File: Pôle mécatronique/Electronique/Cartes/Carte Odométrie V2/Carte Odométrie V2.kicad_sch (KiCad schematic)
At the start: 10 parts, among them J1 Conn_01x05, J2 Conn_01x08, J3 Conn_01x07, J4 Conn_01x04, J5 Conn_01x07, J6 Conn_01x04, U1 TCAN332

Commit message: MAJ carte actionneur
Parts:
- removed U1: TCAN332, empreinte:SO-8_S, symbol Interface_CAN_LIN:TCAN332
- added C1, C2: C, Capacitor_SMD:C_1206_3216Metric, symbol Device:C
- added R3: R, Resistor_THT:R_Axial_DIN0207_L6.3mm_D2.5mm_P10.16mm_Horizontal, symbol Device:R
- added TP1: TestPoint, TestPoint:TestPoint_Pad_D2.0mm, symbol Connector:TestPoint
- added U1: MCP2551-I-P, Package_DIP:DIP-8_W7.62mm, symbol Interface_CAN_LIN:MCP2551-I-P
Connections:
- net +5V: now also J4.4 (Pin_4), C1.1, C2.1, U1.3 (VDD)
- net CAN_H: now also R3.1, U1.7 (CANH)
- net CAN_L: now also R3.2, U1.6 (CANL)
- net CAN_RX: now also U1.4 (RXD)
- net CAN_TX: now also U1.1 (TXD)
- net GND: now also C1.2, C2.2, TP1.1, U1.2 (VSS), U1.8 (Rs)
- net +BATT: no longer names the net of A1.4.1 (VIN)
- net +BATT: no longer J4.4 (Pin_4)
- no-connect marks 23 -> 25

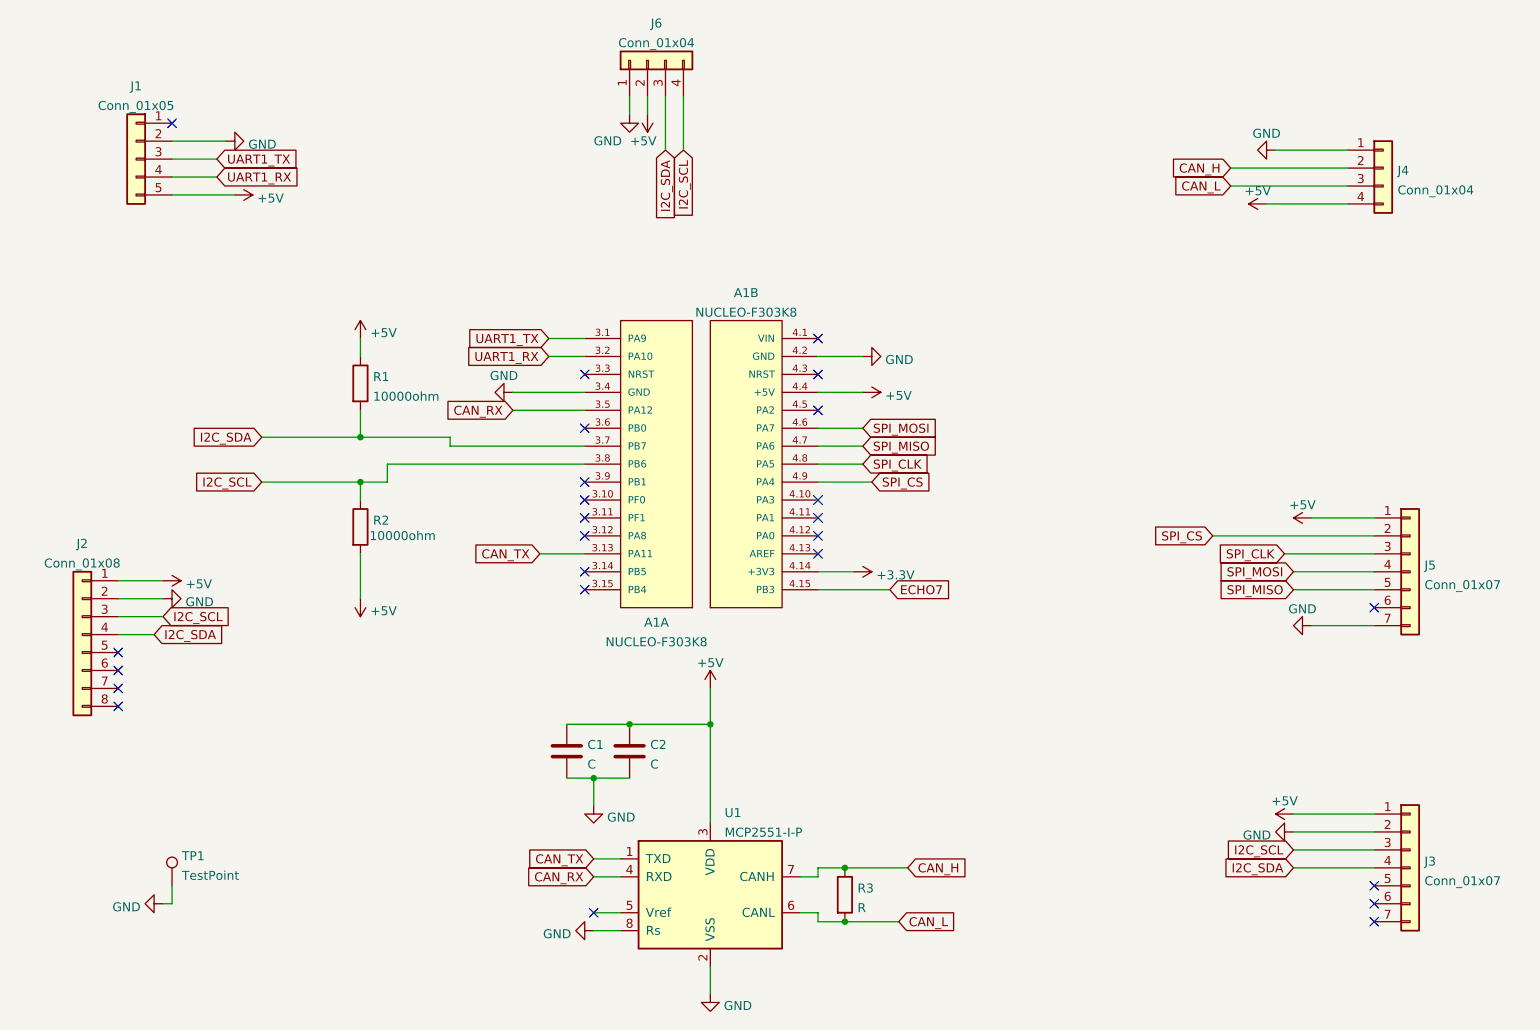
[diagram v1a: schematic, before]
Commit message: Sérigraphie Carte
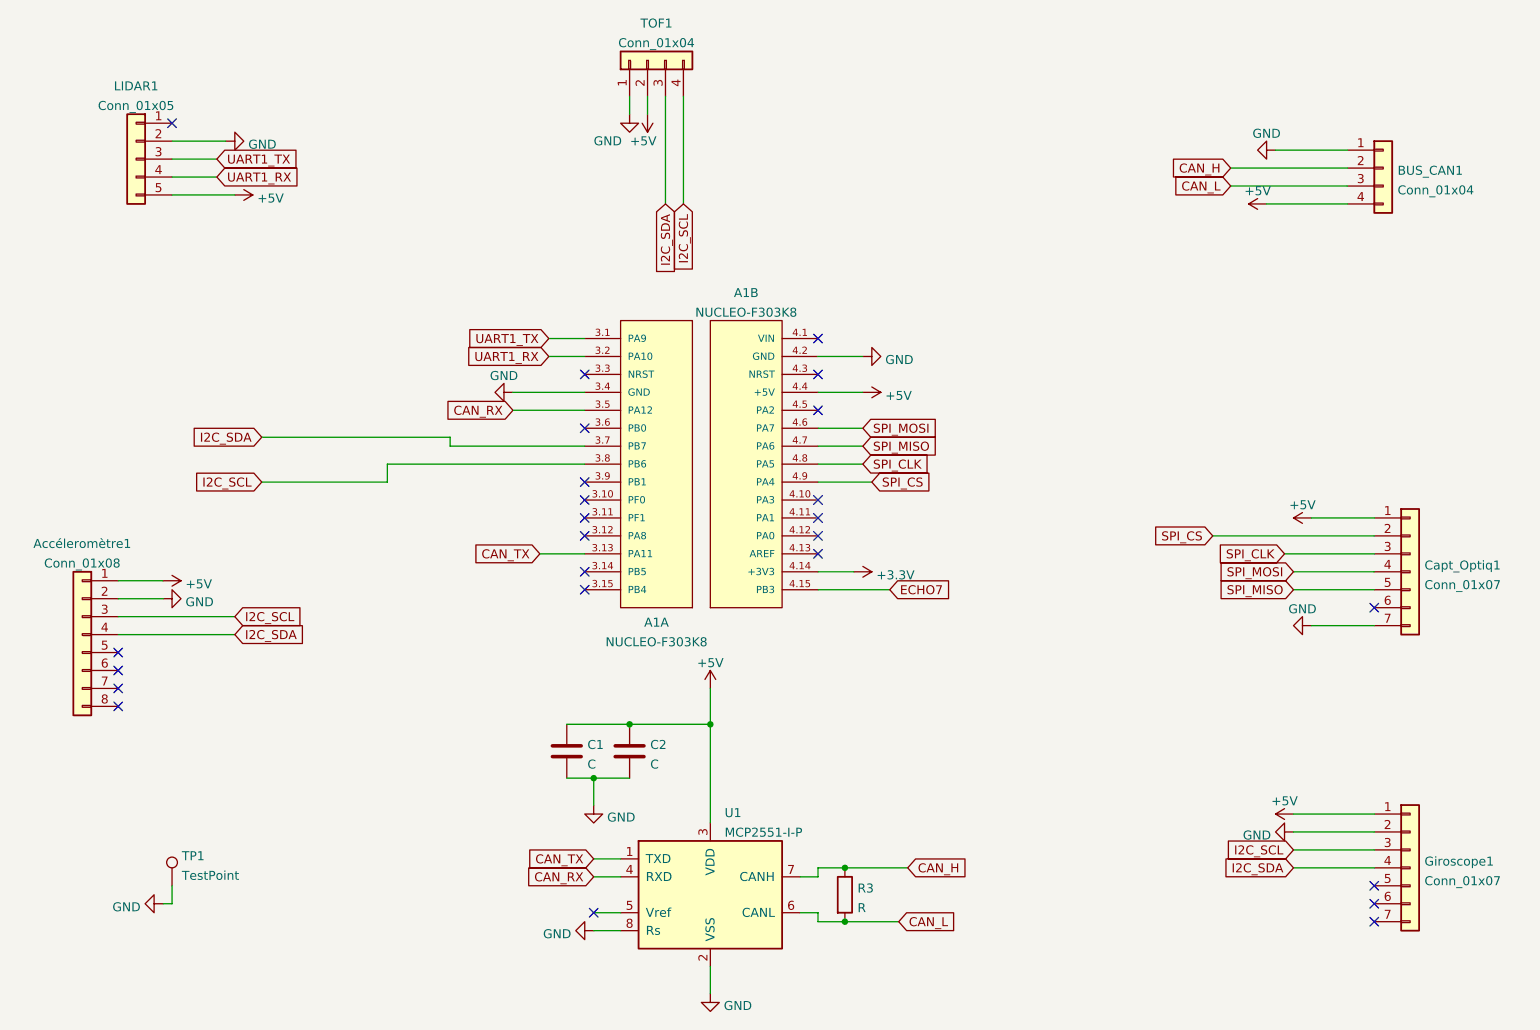
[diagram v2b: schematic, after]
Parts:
- removed R1, R2: 10000ohm, Resistor_THT:R_Axial_DIN0207_L6.3mm_D2.5mm_P10.16mm_Horizontal, symbol Device:R
- renumbered J2 to Accéleromètre1, J4 to BUS_CAN1, J5 to Capt_Optiq1, J3 to Giroscope1, J1 to LIDAR1, J6 to TOF1

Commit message: maj final carte normalement
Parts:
- added +5V1, I2C_SCL1, I2C_SDA1, LID_RX1, LID_TX1, TP1, TP2: TestPoint, TestPoint:TestPoint_Pad_D2.0mm, symbol Connector:TestPoint
- added C3, C4: C, Capacitor_SMD:C_1206_3216Metric, symbol Device:C
- renumbered TP1 to GND1
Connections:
- net +5V: now also +5V1.1, C3.2, C4.2
- net CAN_H: now also TP1.1
- net CAN_L: now also TP2.1
- net GND: now also C3.1, C4.1
- net I2C_SCL: now also I2C_SCL1.1
- net I2C_SDA: now also I2C_SDA1.1
- net UART1_RX: now also LID_RX1.1
- net UART1_TX: now also LID_TX1.1
- net ECHO7: no longer names the net of A1.4.15 (PB3)
- no-connect marks 25 -> 26

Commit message: oui
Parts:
- added R1, R2: R, Resistor_THT:R_Axial_DIN0207_L6.3mm_D2.5mm_P10.16mm_Horizontal, symbol Device:R
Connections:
- net +5V: now also R1.1, R2.2
- net I2C_SCL: now also R2.1
- net I2C_SDA: now also R1.2
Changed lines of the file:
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@@
   (junction (at 161.29 143.51) (diameter 0) (color 0 0 0 0)
+  )
+  (junction (at 91.44 81.28) (diameter 0) (color 0 0 0 0)
+  )
+  (junction (at 82.55 74.93) (diameter 0) (color 0 0 0 0)
   )
   (junction (at 165.1 143.51) (diameter 0) (color 0 0 0 0)
@@
     (stroke (width 0) (type default) (color 0 0 0 0))
   )
+  (wire (pts (xy 91.44 81.28) (xy 96.52 81.28))
+    (stroke (width 0) (type default) (color 0 0 0 0))
+  )
   (wire (pts (xy 224.79 96.52) (xy 236.22 96.52))
     (stroke (width 0) (type default) (color 0 0 0 0))
   )
+  (wire (pts (xy 82.55 74.93) (xy 105.41 74.93))
+    (stroke (width 0) (type default) (color 0 0 0 0))
+  )
   (wire (pts (xy 163.83 68.58) (xy 163.83 69.85))
     (stroke (width 0) (type default) (color 0 0 0 0))
@@
     (stroke (width 0) (type default) (color 0 0 0 0))
   )
+  (wire (pts (xy 82.55 58.42) (xy 82.55 67.31))
+    (stroke (width 0) (type default) (color 0 0 0 0))
+  )
   (wire (pts (xy 125.73 142.24) (xy 129.54 142.24))
     (stroke (width 0) (type default) (color 0 0 0 0))
@@
     (stroke (width 0) (type default) (color 0 0 0 0))
   )
+  (wire (pts (xy 91.44 88.9) (xy 91.44 91.44))
+    (stroke (width 0) (type default) (color 0 0 0 0))
+  )
   (wire (pts (xy 142.24 115.57) (xy 142.24 129.54))
     (stroke (width 0) (type default) (color 0 0 0 0))
@@
     (stroke (width 0) (type default) (color 0 0 0 0))
   )
-  (wire (pts (xy 78.74 81.28) (xy 96.52 81.28))
+  (wire (pts (xy 78.74 81.28) (xy 91.44 81.28))
     (stroke (width 0) (type default) (color 0 0 0 0))
   )
@@
     (stroke (width 0) (type default) (color 0 0 0 0))
   )
-  (wire (pts (xy 78.74 74.93) (xy 105.41 74.93))
+  (wire (pts (xy 78.74 74.93) (xy 82.55 74.93))
     (stroke (width 0) (type default) (color 0 0 0 0))
   )
@@
     (pin "1")
   )
+  (symbol (lib_id "Device:R") (at 82.55 71.12 0) (unit 1)
+    (in_bom yes) (on_board yes) (fields_autoplaced)
+    (property "Reference" "R1" (id 0) (at 84.328 70.2115 0)
+      (effects (font (size 1.27 1.27)) (justify left))
+    )
+    (property "Value" "R" (id 1) (at 84.328 72.9866 0)
+      (effects (font (size 1.27 1.27)) (justify left))
+    )
+    (property "Footprint" "Resistor_THT:R_Axial_DIN0207_L6.3mm_D2.5mm_P10.16mm_Horizontal" (id 2) (at 80.772 71.12 90)
+      (effects (font (size 1.27 1.27)) hide)
+    )
+    (property "Datasheet" "~" (id 3) (at 82.55 71.12 0)
+      (effects (font (size 1.27 1.27)) hide)
+    )
+    (pin "1")
+    (pin "2")
+  )
   (symbol (lib_id "Connector_Generic:Conn_01x08") (at 53.34 102.87 0) (mirror y) (unit 1)
     (in_bom yes) (on_board yes) (fields_autoplaced)
@@
     (pin "1")
   )
+  (symbol (lib_id "Device:R") (at 91.44 85.09 0) (unit 1)
+    (in_bom yes) (on_board yes) (fields_autoplaced)
+    (property "Reference" "R2" (id 0) (at 93.218 84.1815 0)
+      (effects (font (size 1.27 1.27)) (justify left))
+    )
+    (property "Value" "R" (id 1) (at 93.218 86.9566 0)
+      (effects (font (size 1.27 1.27)) (justify left))
+    )
+    (property "Footprint" "Resistor_THT:R_Axial_DIN0207_L6.3mm_D2.5mm_P10.16mm_Horizontal" (id 2) (at 89.662 85.09 90)
+      (effects (font (size 1.27 1.27)) hide)
+    )
+    (property "Datasheet" "~" (id 3) (at 91.44 85.09 0)
+      (effects (font (size 1.27 1.27)) hide)
+    )
+    (pin "1")
+    (pin "2")
+  )
   (symbol (lib_id "power:GND") (at 179.07 62.23 90) (unit 1)
     (in_bom yes) (on_board yes) (fields_autoplaced)
@@
     )
     (property "Datasheet" "" (id 3) (at 179.07 62.23 0)
+      (effects (font (size 1.27 1.27)) hide)
+    )
+    (pin "1")
+  )
+  (symbol (lib_id "power:+5V") (at 82.55 58.42 0) (mirror y) (unit 1)
+    (in_bom yes) (on_board yes)
+    (property "Reference" "#PWR0103" (id 0) (at 82.55 62.23 0)
+      (effects (font (size 1.27 1.27)) hide)
+    )
+    (property "Value" "+5V" (id 1) (at 81.28 54.61 0)
+      (effects (font (size 1.27 1.27)) (justify right))
+    )
+    (property "Footprint" "" (id 2) (at 82.55 58.42 0)
+      (effects (font (size 1.27 1.27)) hide)
+    )
+    (property "Datasheet" "" (id 3) (at 82.55 58.42 0)
       (effects (font (size 1.27 1.27)) hide)
     )
@@
     )
     (property "Datasheet" "~" (id 3) (at 135.89 33.02 0)
+      (effects (font (size 1.27 1.27)) hide)
+    )
+    (pin "1")
+  )
+  (symbol (lib_id "power:+5V") (at 91.44 91.44 0) (mirror x) (unit 1)
+    (in_bom yes) (on_board yes)
+    (property "Reference" "#PWR0102" (id 0) (at 91.44 87.63 0)
+      (effects (font (size 1.27 1.27)) hide)
+    )
+    (property "Value" "+5V" (id 1) (at 92.71 95.25 0)
+      (effects (font (size 1.27 1.27)) (justify right))
+    )
+    (property "Footprint" "" (id 2) (at 91.44 91.44 0)
+      (effects (font (size 1.27 1.27)) hide)
+    )
+    (property "Datasheet" "" (id 3) (at 91.44 91.44 0)
       (effects (font (size 1.27 1.27)) hide)
     )
@@
       (reference "#PWR0101") (unit 1) (value "GND") (footprint "")
     )
+    (path "/8ba9c3fb-46f6-4875-a664-e313ccfeba0c"
+      (reference "#PWR0102") (unit 1) (value "+5V") (footprint "")
+    )
+    (path "/5a7a8c16-813c-4d39-bb38-4fe8173d3667"
+      (reference "#PWR0103") (unit 1) (value "+5V") (footprint "")
+    )
     (path "/2ff1eef4-c959-45e1-8edc-bfa0a58f8f61"
       (reference "#PWR0104") (unit 1) (value "+3.3V") (footprint "")
@@
       (reference "LID_TX1") (unit 1) (value "TestPoint") (footprint "TestPoint:TestPoint_Pad_D2.0mm")
     )
+    (path "/34f66f22-45b2-4607-96e4-1850e941d14c"
+      (reference "R1") (unit 1) (value "R") (footprint "Resistor_THT:R_Axial_DIN0207_L6.3mm_D2.5mm_P10.16mm_Horizontal")
+    )
+    (path "/494350ab-d17d-4de3-8b96-f15451154d6a"
+      (reference "R2") (unit 1) (value "R") (footprint "Resistor_THT:R_Axial_DIN0207_L6.3mm_D2.5mm_P10.16mm_Horizontal")
+    )
     (path "/40b1f97f-e04b-4d3c-b960-bed063aa2f91"

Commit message: carte odo
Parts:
- added Can_RX1, Can_TX1, SPI_CLK1, SPI_CS1, SPI_MISO1, SPI_MOSI1: TestPoint, TestPoint:TestPoint_Pad_D2.0mm, symbol Connector:TestPoint
- renumbered TP1 to Can_H1, TP2 to Can_L1
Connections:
- net CAN_RX: now also Can_RX1.1
- net CAN_TX: now also Can_TX1.1
- net SPI_CLK: now also SPI_CLK1.1
- net SPI_CS: now also SPI_CS1.1
- net SPI_MISO: now also SPI_MISO1.1
- net SPI_MOSI: now also SPI_MOSI1.1

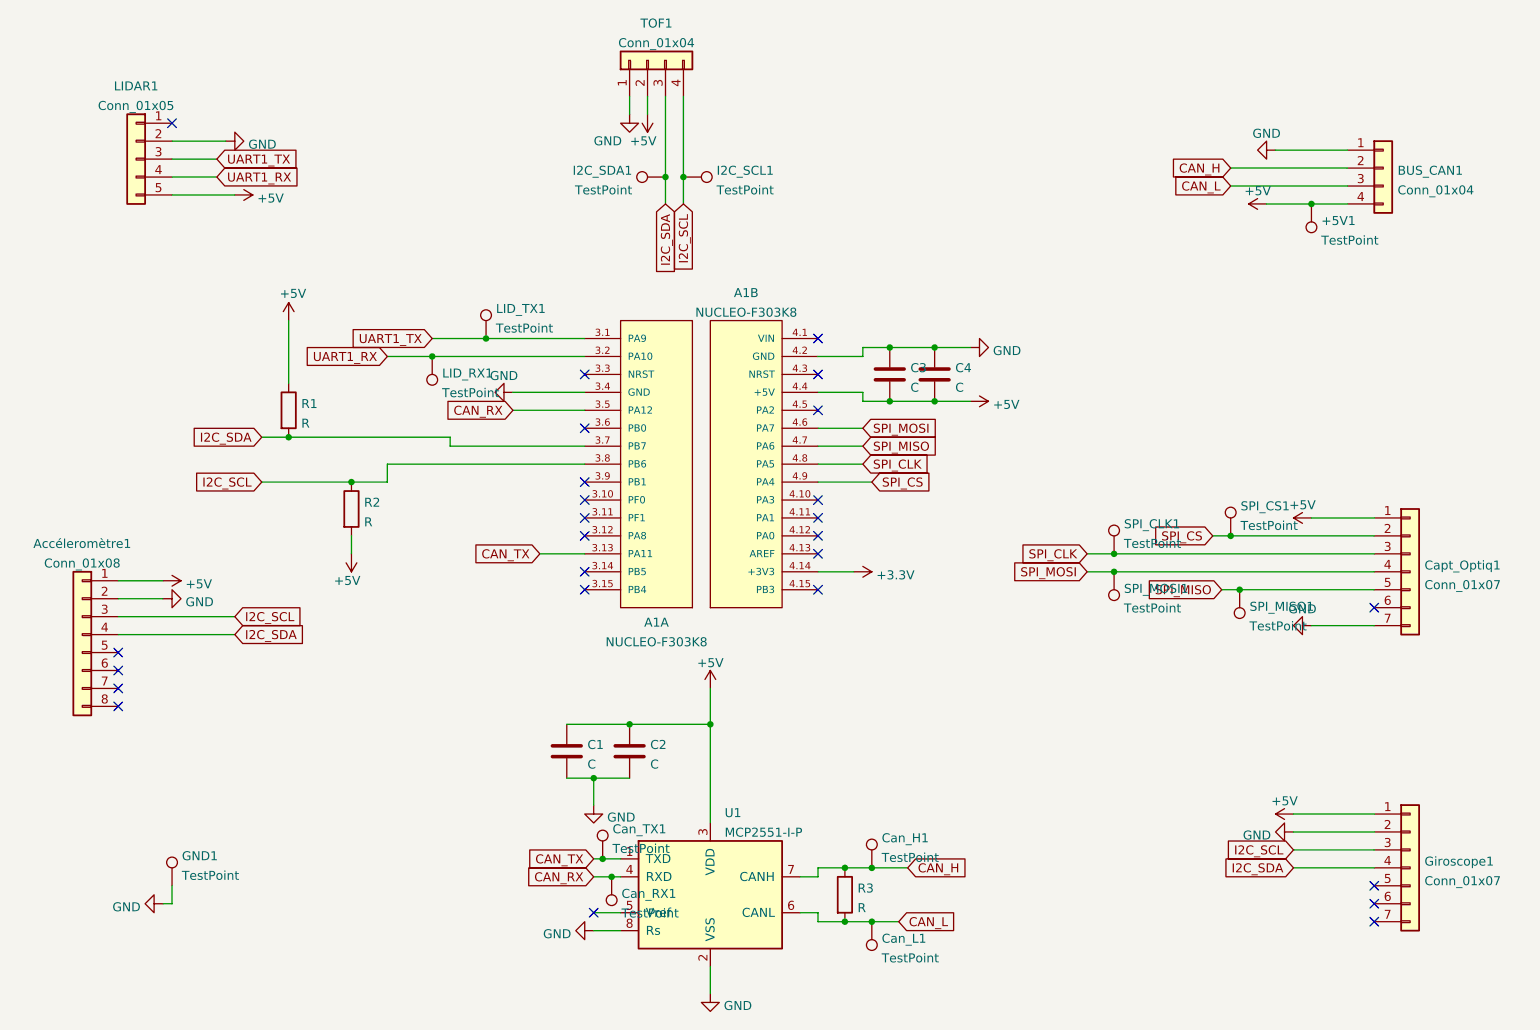
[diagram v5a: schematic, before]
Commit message: Xshut carte Odo
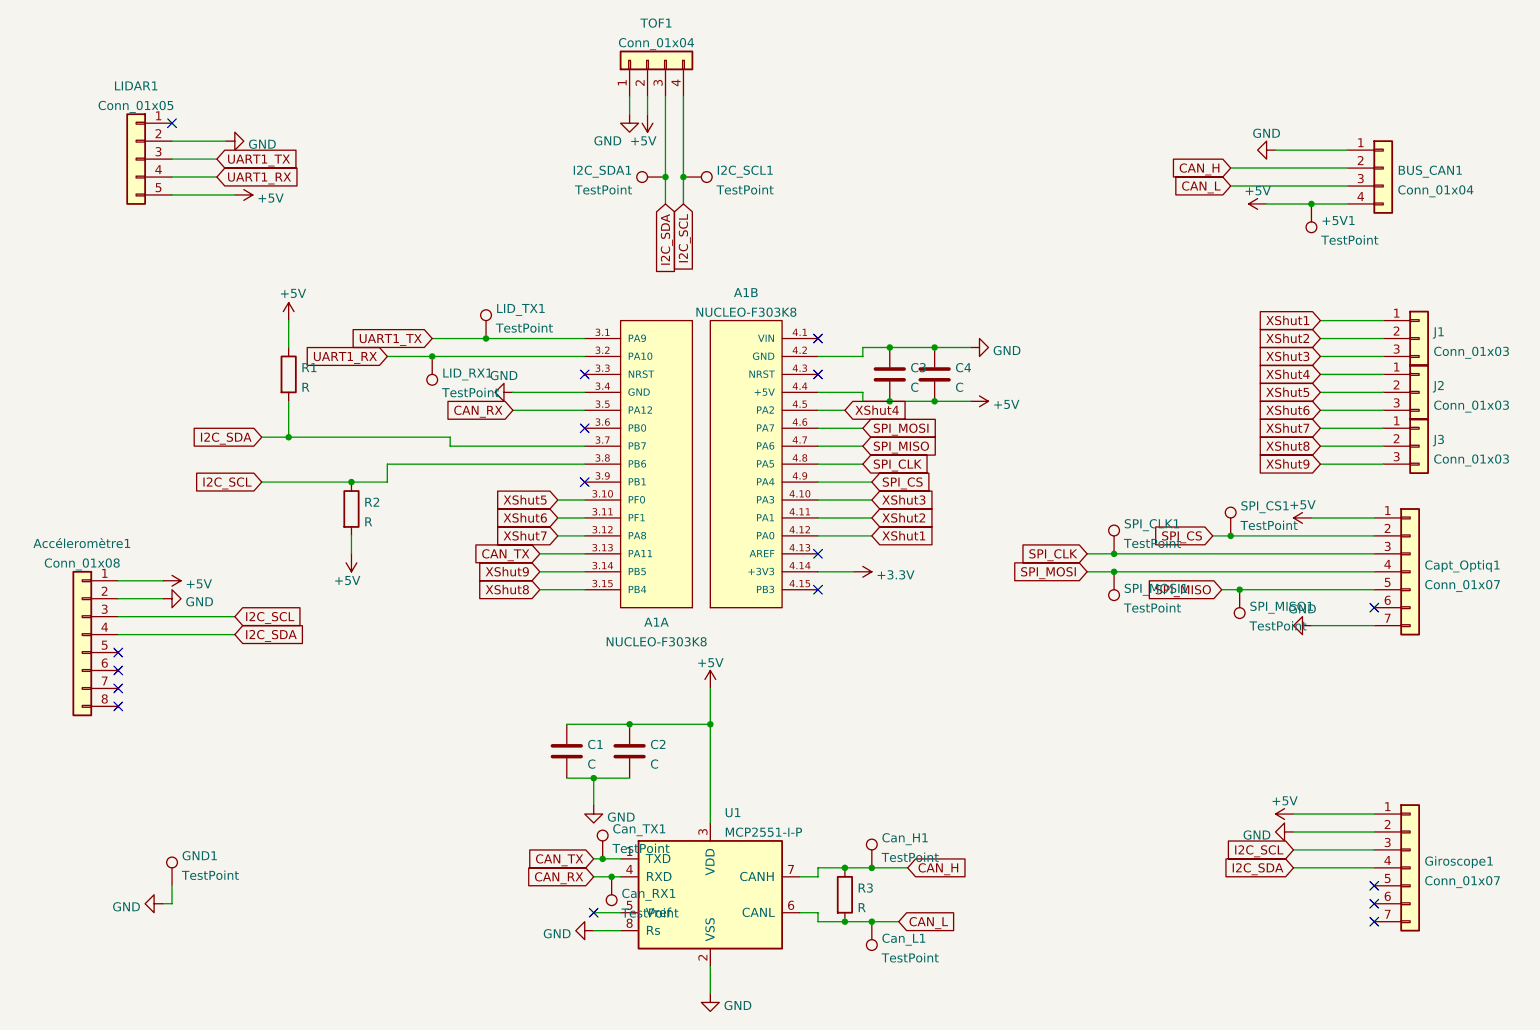
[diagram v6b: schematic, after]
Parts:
- added J1, J2, J3: Conn_01x03, Connector_JST:JST_EH_B3B-EH-A_1x03_P2.50mm_Vertical, symbol Connector_Generic:Conn_01x03
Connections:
- net XShut3: now reaches A1.4.10 (PA3)
- net XShut3: now also J1.3 (Pin_3)
- net XShut2: now reaches A1.4.11 (PA1)
- net XShut2: now also J1.2 (Pin_2)
- net XShut1: now reaches A1.4.12 (PA0)
- net XShut1: now also J1.1 (Pin_1)
- net XShut4: now reaches A1.4.5 (PA2)
- net XShut4: now also J2.1 (Pin_1)
- net XShut5: now reaches A1.3.10 (PF0)
- net XShut5: now also J2.2 (Pin_2)
- net XShut6: now reaches A1.3.11 (PF1)
- net XShut6: now also J2.3 (Pin_3)
- net XShut7: now reaches A1.3.12 (PA8)
- net XShut7: now also J3.1 (Pin_1)
- net XShut9: now reaches A1.3.14 (PB5)
- net XShut9: now also J3.3 (Pin_3)
- net XShut8: now reaches A1.3.15 (PB4)
- net XShut8: now also J3.2 (Pin_2)
- no-connect marks 26 -> 17
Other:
- moved on the sheet: R1
